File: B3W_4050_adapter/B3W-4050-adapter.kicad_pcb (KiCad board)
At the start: 2 copper layers, 16.2 x 12.5 mm, 5 parts, among them P1 CONN_01X01, P2 CONN_01X01, P3 CONN_01X01, P4 CONN_01X01, SW1 B3W-4050

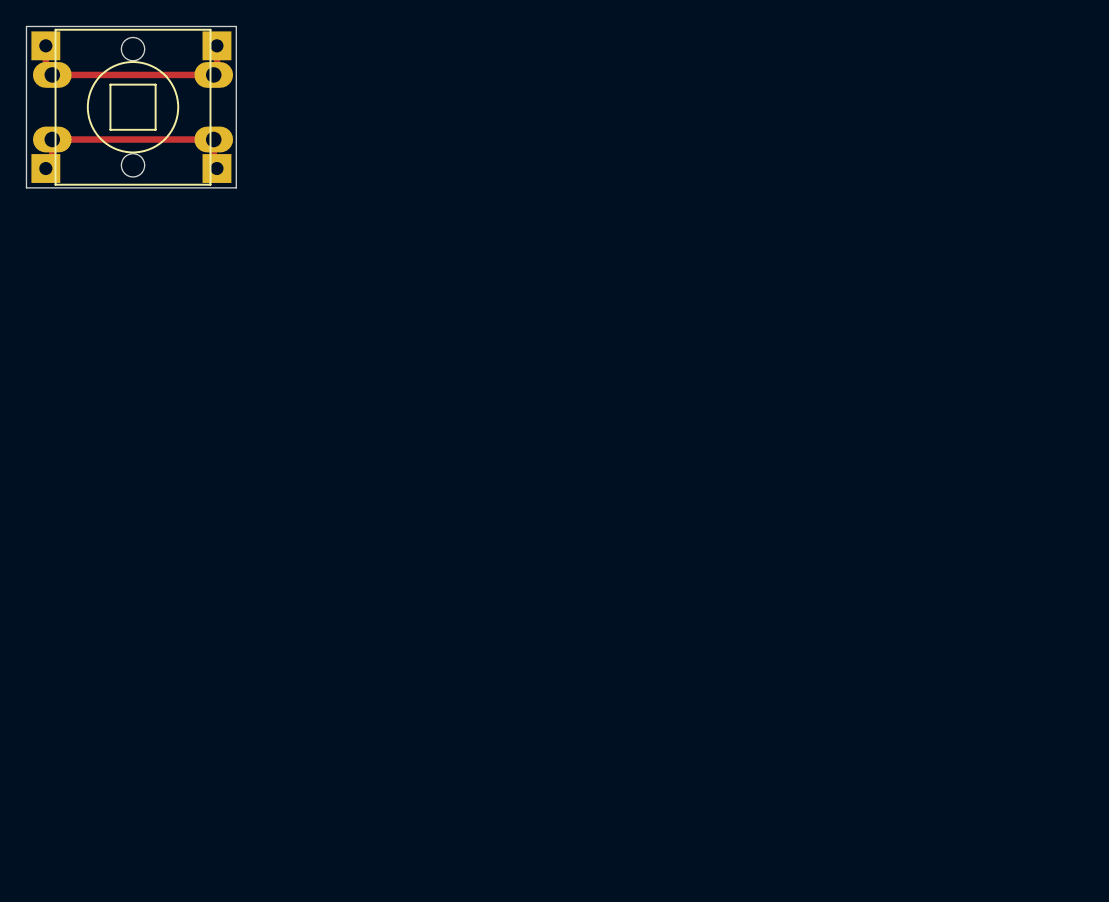
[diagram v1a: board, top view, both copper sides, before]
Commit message: panelizing 4050 switch adapter pcb
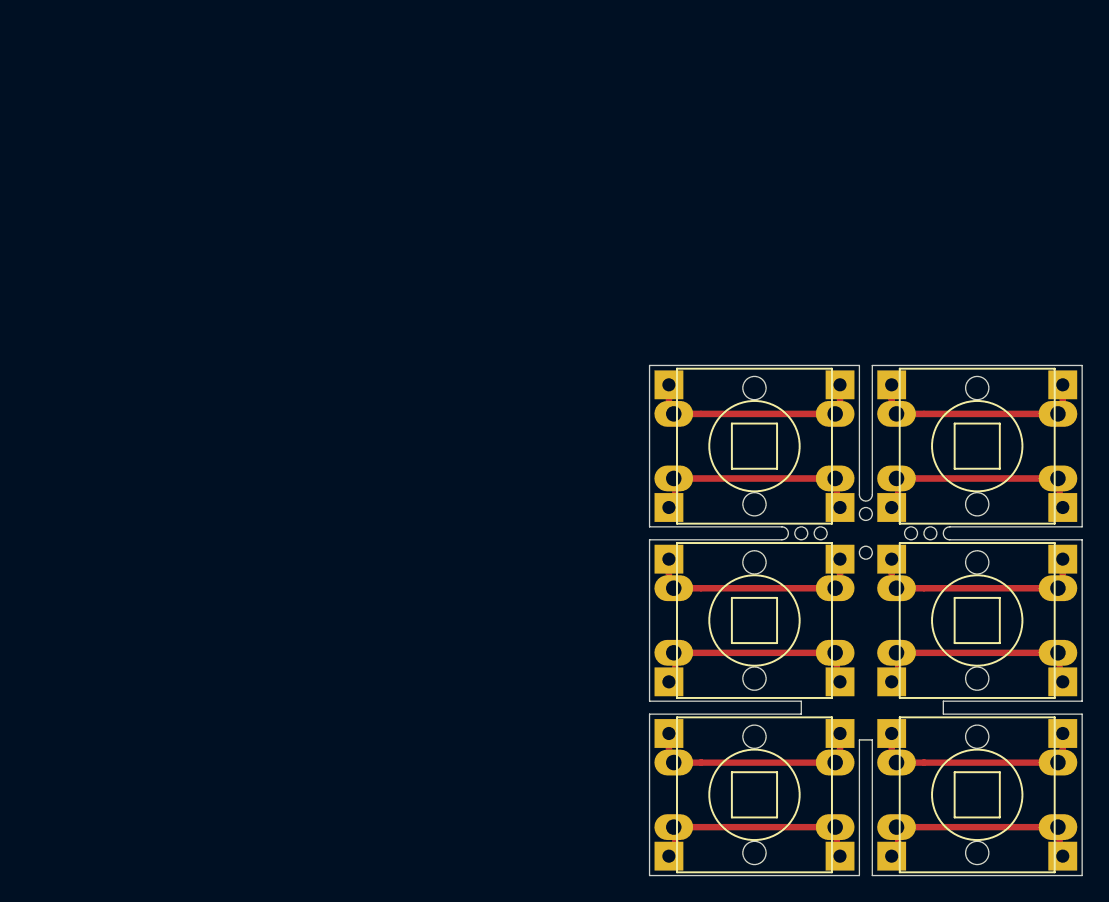
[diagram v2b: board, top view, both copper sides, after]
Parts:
- added HOLE-0.125-INCH: VAL**, MyModules:HOLE-0.125-INCH, F.Cu at (56.8, 34.5)
- added HOLE-0.125-INCH: VAL**, MyModules:HOLE-0.125-INCH, F.Cu at (61.8, 33.0)
- added HOLE-0.125-INCH: VAL**, MyModules:HOLE-0.125-INCH, F.Cu at (60.2, 33.0)
- added HOLE-0.125-INCH: VAL**, MyModules:HOLE-0.125-INCH, F.Cu at (51.8, 33.0)
- added HOLE-0.125-INCH: VAL**, MyModules:HOLE-0.125-INCH, F.Cu at (53.2, 33.0)
- added HOLE-0.125-INCH: VAL**, MyModules:HOLE-0.125-INCH, F.Cu at (56.8, 33.0)
- added HOLE-0.125-INCH: VAL**, MyModules:HOLE-0.125-INCH, F.Cu at (56.8, 31.5)
- added HOLE-0.125-INCH: VAL**, MyModules:HOLE-0.125-INCH, F.Cu at (56.8, 39.8)
- added P1: CONN_01X01, Pin_Headers:Pin_Header_Straight_1x01, B.Cu at (72.0, 58.0)
- added P1: CONN_01X01, Pin_Headers:Pin_Header_Straight_1x01, B.Cu at (54.8, 58.0)
- added P1: CONN_01X01, Pin_Headers:Pin_Header_Straight_1x01, B.Cu at (72.0, 44.5)
- added P1: CONN_01X01, Pin_Headers:Pin_Header_Straight_1x01, B.Cu at (54.8, 44.5)
- added P1: CONN_01X01, Pin_Headers:Pin_Header_Straight_1x01, B.Cu at (72.0, 31.0)
- added P2: CONN_01X01, Pin_Headers:Pin_Header_Straight_1x01, B.Cu at (58.8, 58.0)
- added P2: CONN_01X01, Pin_Headers:Pin_Header_Straight_1x01, B.Cu at (41.5, 58.0)
- added P2: CONN_01X01, Pin_Headers:Pin_Header_Straight_1x01, B.Cu at (58.8, 44.5)
- added P2: CONN_01X01, Pin_Headers:Pin_Header_Straight_1x01, B.Cu at (41.5, 44.5)
- added P2: CONN_01X01, Pin_Headers:Pin_Header_Straight_1x01, B.Cu at (58.8, 31.0)
- added P3: CONN_01X01, Pin_Headers:Pin_Header_Straight_1x01, B.Cu at (72.0, 48.5)
- added P3: CONN_01X01, Pin_Headers:Pin_Header_Straight_1x01, B.Cu at (54.8, 48.5)
- added P3: CONN_01X01, Pin_Headers:Pin_Header_Straight_1x01, B.Cu at (72.0, 35.0)
- added P3: CONN_01X01, Pin_Headers:Pin_Header_Straight_1x01, B.Cu at (54.8, 35.0)
- added P3: CONN_01X01, Pin_Headers:Pin_Header_Straight_1x01, B.Cu at (72.0, 21.5)
- added P4: CONN_01X01, Pin_Headers:Pin_Header_Straight_1x01, B.Cu at (58.8, 48.5)
- added P4: CONN_01X01, Pin_Headers:Pin_Header_Straight_1x01, B.Cu at (41.5, 48.5)
- added P4: CONN_01X01, Pin_Headers:Pin_Header_Straight_1x01, B.Cu at (58.8, 35.0)
- added P4: CONN_01X01, Pin_Headers:Pin_Header_Straight_1x01, B.Cu at (41.5, 35.0)
- added P4: CONN_01X01, Pin_Headers:Pin_Header_Straight_1x01, B.Cu at (58.8, 21.5)
- added SW1: B3W-4050, MyModules:BF-4050-OMRON, F.Cu at (65.4, 53.2)
- added SW1: B3W-4050, MyModules:BF-4050-OMRON, F.Cu at (48.1, 53.2)
- added SW1: B3W-4050, MyModules:BF-4050-OMRON, F.Cu at (65.4, 39.8)
- added SW1: B3W-4050, MyModules:BF-4050-OMRON, F.Cu at (48.1, 39.8)
- added SW1: B3W-4050, MyModules:BF-4050-OMRON, F.Cu at (65.4, 26.2)
- moved P1 54.9 mm to (54.8, 31.0)
- moved P2 54.9 mm to (41.5, 31.0)
- moved P3 54.9 mm to (54.8, 21.5)
- moved P4 54.9 mm to (41.5, 21.5)
- moved SW1 54.8 mm to (48.1, 26.2)
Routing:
- net Net-(P3-Pad1): track 17.3 -> 103.9 mm
- net Net-(P1-Pad1): track 17.3 -> 103.8 mm
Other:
- board size 16.2 x 12.5 mm -> 33.5 x 39.5 mm

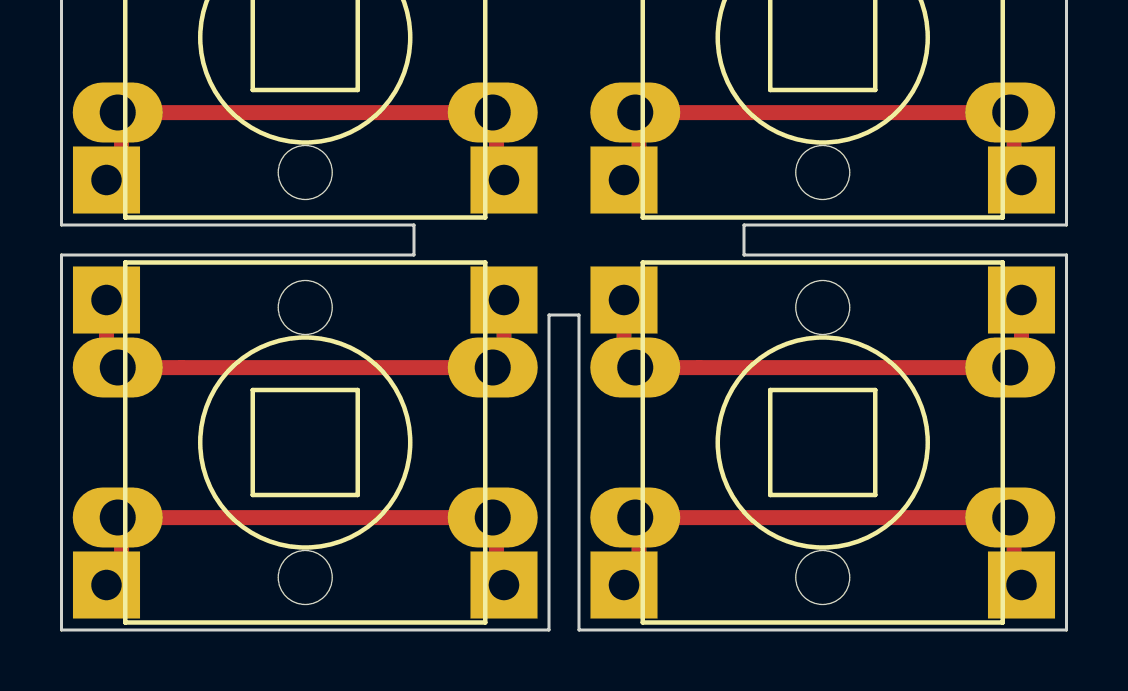
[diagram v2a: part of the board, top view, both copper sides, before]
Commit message: finished panelizing 4050 switch adapter board
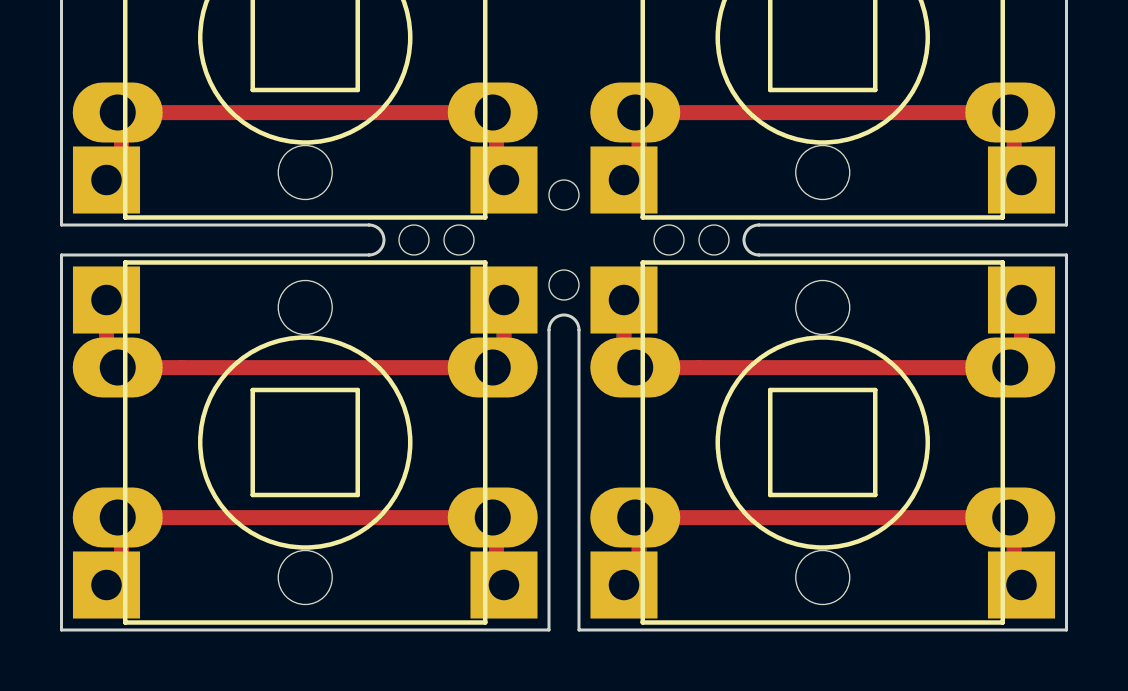
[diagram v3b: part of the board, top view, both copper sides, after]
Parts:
- added HOLE-0.125-INCH: VAL**, MyModules:HOLE-0.125-INCH, F.Cu at (56.8, 48.0)
- added HOLE-0.125-INCH: VAL**, MyModules:HOLE-0.125-INCH, F.Cu at (61.8, 46.5)
- added HOLE-0.125-INCH: VAL**, MyModules:HOLE-0.125-INCH, F.Cu at (60.2, 46.5)
- added HOLE-0.125-INCH: VAL**, MyModules:HOLE-0.125-INCH, F.Cu at (56.8, 46.5)
- added HOLE-0.125-INCH: VAL**, MyModules:HOLE-0.125-INCH, F.Cu at (56.8, 45.0)
- added HOLE-0.125-INCH: VAL**, MyModules:HOLE-0.125-INCH, F.Cu at (53.2, 46.5)
- added HOLE-0.125-INCH: VAL**, MyModules:HOLE-0.125-INCH, F.Cu at (51.8, 46.5)
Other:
- outline, holes or cut-outs redrawn
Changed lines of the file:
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@@
     (tracks 66)
     (zones 0)
-    (modules 38)
+    (modules 45)
     (nets 3)
   )
@@
   )
   (module MyModules:HOLE-0.125-INCH (layer F.Cu)
+    (at 56.75 48)
+    (fp_text reference HOLE-0.125-INCH (at 0 -5) (layer F.SilkS) hide
+      (effects (font (size 1.5 1.5) (thickness 0.15)))
+    )
+    (fp_text value VAL** (at 0 5) (layer F.SilkS) hide
+      (effects (font (size 1.5 1.5) (thickness 0.15)))
+    )
+    (pad "" np_thru_hole oval (at 0 0) (size 1 1) (drill oval 1) (layers *.Cu *.Mask F.SilkS))
+  )
+  (module MyModules:HOLE-0.125-INCH (layer F.Cu)
+    (at 61.75 46.5)
+    (fp_text reference HOLE-0.125-INCH (at 0 -5) (layer F.SilkS) hide
+      (effects (font (size 1.5 1.5) (thickness 0.15)))
+    )
+    (fp_text value VAL** (at 0 5) (layer F.SilkS) hide
+      (effects (font (size 1.5 1.5) (thickness 0.15)))
+    )
+    (pad "" np_thru_hole oval (at 0 0) (size 1 1) (drill oval 1) (layers *.Cu *.Mask F.SilkS))
+  )
+  (module MyModules:HOLE-0.125-INCH (layer F.Cu)
+    (at 60.25 46.5)
+    (fp_text reference HOLE-0.125-INCH (at 0 -5) (layer F.SilkS) hide
+      (effects (font (size 1.5 1.5) (thickness 0.15)))
+    )
+    (fp_text value VAL** (at 0 5) (layer F.SilkS) hide
+      (effects (font (size 1.5 1.5) (thickness 0.15)))
+    )
+    (pad "" np_thru_hole oval (at 0 0) (size 1 1) (drill oval 1) (layers *.Cu *.Mask F.SilkS))
+  )
+  (module MyModules:HOLE-0.125-INCH (layer F.Cu)
+    (at 56.75 46.5)
+    (fp_text reference HOLE-0.125-INCH (at 0 -5) (layer F.SilkS) hide
+      (effects (font (size 1.5 1.5) (thickness 0.15)))
+    )
+    (fp_text value VAL** (at 0 5) (layer F.SilkS) hide
+      (effects (font (size 1.5 1.5) (thickness 0.15)))
+    )
+    (pad "" np_thru_hole oval (at 0 0) (size 4 1) (drill oval 4 1) (layers *.Cu *.Mask F.SilkS))
+  )
+  (module MyModules:HOLE-0.125-INCH (layer F.Cu)
+    (at 56.75 45)
+    (fp_text reference HOLE-0.125-INCH (at 0 -5) (layer F.SilkS) hide
+      (effects (font (size 1.5 1.5) (thickness 0.15)))
+    )
+    (fp_text value VAL** (at 0 5) (layer F.SilkS) hide
+      (effects (font (size 1.5 1.5) (thickness 0.15)))
+    )
+    (pad "" np_thru_hole oval (at 0 0) (size 1 1) (drill oval 1) (layers *.Cu *.Mask F.SilkS))
+  )
+  (module MyModules:HOLE-0.125-INCH (layer F.Cu)
+    (at 53.25 46.5)
+    (fp_text reference HOLE-0.125-INCH (at 0 -5) (layer F.SilkS) hide
+      (effects (font (size 1.5 1.5) (thickness 0.15)))
+    )
+    (fp_text value VAL** (at 0 5) (layer F.SilkS) hide
+      (effects (font (size 1.5 1.5) (thickness 0.15)))
+    )
+    (pad "" np_thru_hole oval (at 0 0) (size 1 1) (drill oval 1) (layers *.Cu *.Mask F.SilkS))
+  )
+  (module MyModules:HOLE-0.125-INCH (layer F.Cu)
+    (at 51.75 46.5)
+    (fp_text reference HOLE-0.125-INCH (at 0 -5) (layer F.SilkS) hide
+      (effects (font (size 1.5 1.5) (thickness 0.15)))
+    )
+    (fp_text value VAL** (at 0 5) (layer F.SilkS) hide
+      (effects (font (size 1.5 1.5) (thickness 0.15)))
+    )
+    (pad "" np_thru_hole oval (at 0 0) (size 1 1) (drill oval 1) (layers *.Cu *.Mask F.SilkS))
+  )
+  (module MyModules:HOLE-0.125-INCH (layer F.Cu)
     (at 56.75 34.5)
     (fp_text reference HOLE-0.125-INCH (at 0 -5) (layer F.SilkS) hide
@@
     (pad "" np_thru_hole circle (at 0 4.5) (size 1.8 1.8) (drill 1.8) (layers *.Cu *.Mask F.SilkS))
   )
+  (gr_arc (start 56.75 49.5) (end 56.25 49.5) (angle 180) (layer Edge.Cuts) (width 0.1))
+  (gr_arc (start 63.25 46.5) (end 63.25 47) (angle 180) (layer Edge.Cuts) (width 0.1))
+  (gr_arc (start 50.25 46.5) (end 50.25 46) (angle 180) (layer Edge.Cuts) (width 0.1))
   (gr_arc (start 56.75 30) (end 57.25 30) (angle 180) (layer Edge.Cuts) (width 0.1))
   (gr_arc (start 50.25 33) (end 50.25 32.5) (angle 180) (layer Edge.Cuts) (width 0.1))
@@
   (gr_line (start 57.25 32.5) (end 57.25 20) (angle 90) (layer Eco1.User) (width 0.1))
   (gr_line (start 73.5 20) (end 73.5 32.5) (angle 90) (layer Eco1.User) (width 0.1))
-  (gr_line (start 56.25 49) (end 56.25 59.5) (angle 90) (layer Edge.Cuts) (width 0.1))
-  (gr_line (start 57.25 49) (end 56.25 49) (angle 90) (layer Edge.Cuts) (width 0.1))
-  (gr_line (start 57.25 59.5) (end 57.25 49) (angle 90) (layer Edge.Cuts) (width 0.1))
+  (gr_line (start 56.25 49.5) (end 56.25 59.5) (angle 90) (layer Edge.Cuts) (width 0.1))
+  (gr_line (start 57.25 59.5) (end 57.25 49.5) (angle 90) (layer Edge.Cuts) (width 0.1))
   (gr_line (start 40 59.5) (end 56.25 59.5) (layer Edge.Cuts) (width 0.1))
   (gr_line (start 40 47) (end 40 59.5) (layer Edge.Cuts) (width 0.1))
-  (gr_line (start 51.75 47) (end 40 47) (layer Edge.Cuts) (width 0.1))
-  (gr_line (start 51.75 46) (end 51.75 47) (layer Edge.Cuts) (width 0.1))
-  (gr_line (start 40 46) (end 51.75 46) (layer Edge.Cuts) (width 0.1))
+  (gr_line (start 50.25 47) (end 40 47) (layer Edge.Cuts) (width 0.1))
+  (gr_line (start 40 46) (end 50.25 46) (layer Edge.Cuts) (width 0.1))
   (gr_line (start 40 33.5) (end 40 46) (layer Edge.Cuts) (width 0.1))
   (gr_line (start 40 20) (end 40 32.5) (layer Edge.Cuts) (width 0.1))
@@
   (gr_line (start 73.5 59.5) (end 57.25 59.5) (angle 90) (layer Edge.Cuts) (width 0.1))
   (gr_line (start 73.5 47) (end 73.5 59.5) (angle 90) (layer Edge.Cuts) (width 0.1))
-  (gr_line (start 62.75 47) (end 73.5 47) (angle 90) (layer Edge.Cuts) (width 0.1))
-  (gr_line (start 62.75 46) (end 62.75 47) (angle 90) (layer Edge.Cuts) (width 0.1))
-  (gr_line (start 73.5 46) (end 62.75 46) (angle 90) (layer Edge.Cuts) (width 0.1))
+  (gr_line (start 63.25 47) (end 73.5 47) (angle 90) (layer Edge.Cuts) (width 0.1))
+  (gr_line (start 73.5 46) (end 63.25 46) (angle 90) (layer Edge.Cuts) (width 0.1))
   (gr_line (start 73.5 33.5) (end 73.5 46) (angle 90) (layer Edge.Cuts) (width 0.1))
   (gr_line (start 63.25 33.5) (end 73.5 33.5) (angle 90) (layer Edge.Cuts) (width 0.1))
